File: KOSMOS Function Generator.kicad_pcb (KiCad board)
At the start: 2 copper layers, 96 x 125.6 mm, 96 parts, among them J1 Synth_power_2x5, J2 Conn_01x10_Male, Q1 2N3904, Q2 2N3904, SW1 SW_SPDT, SW2 SW_DPDT_x2, SW3 SW_Push, U1 TL074, U2 TL074, U3 TL074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

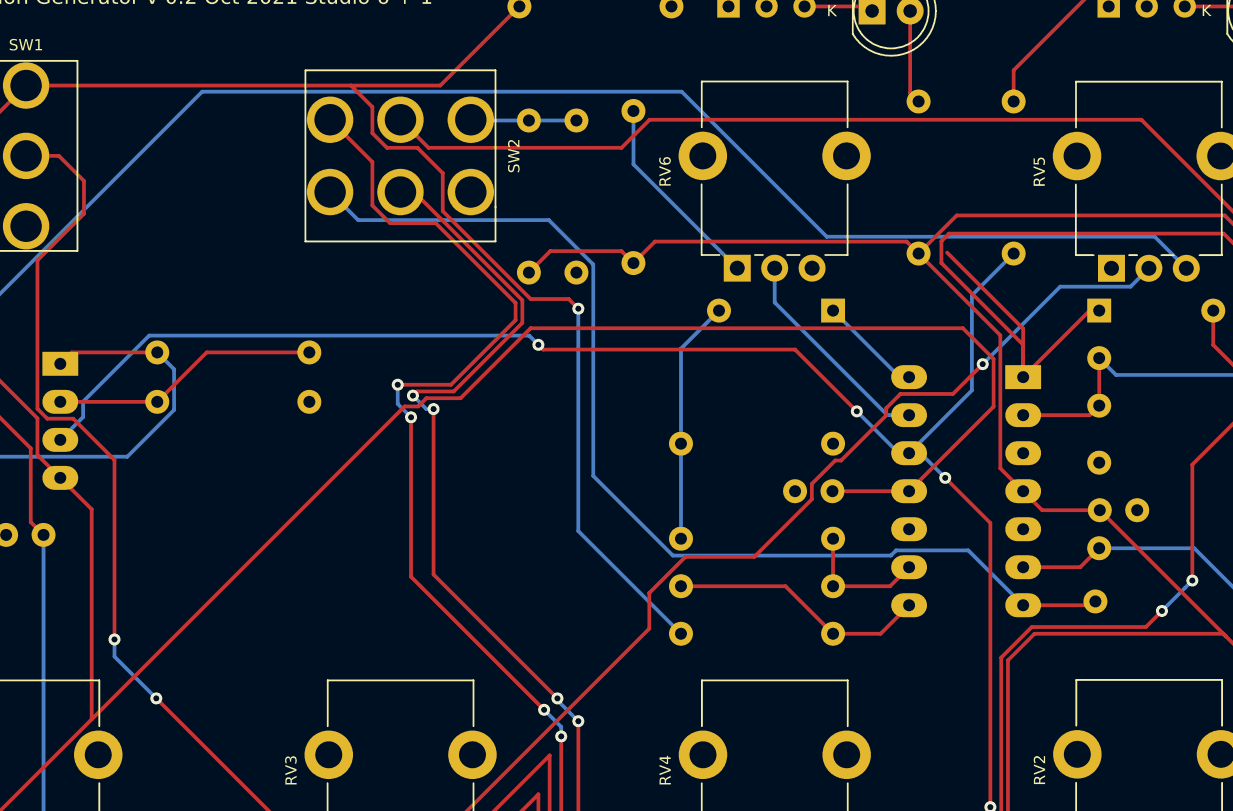
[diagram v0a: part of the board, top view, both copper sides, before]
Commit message: v03 pcb connect ground plane region
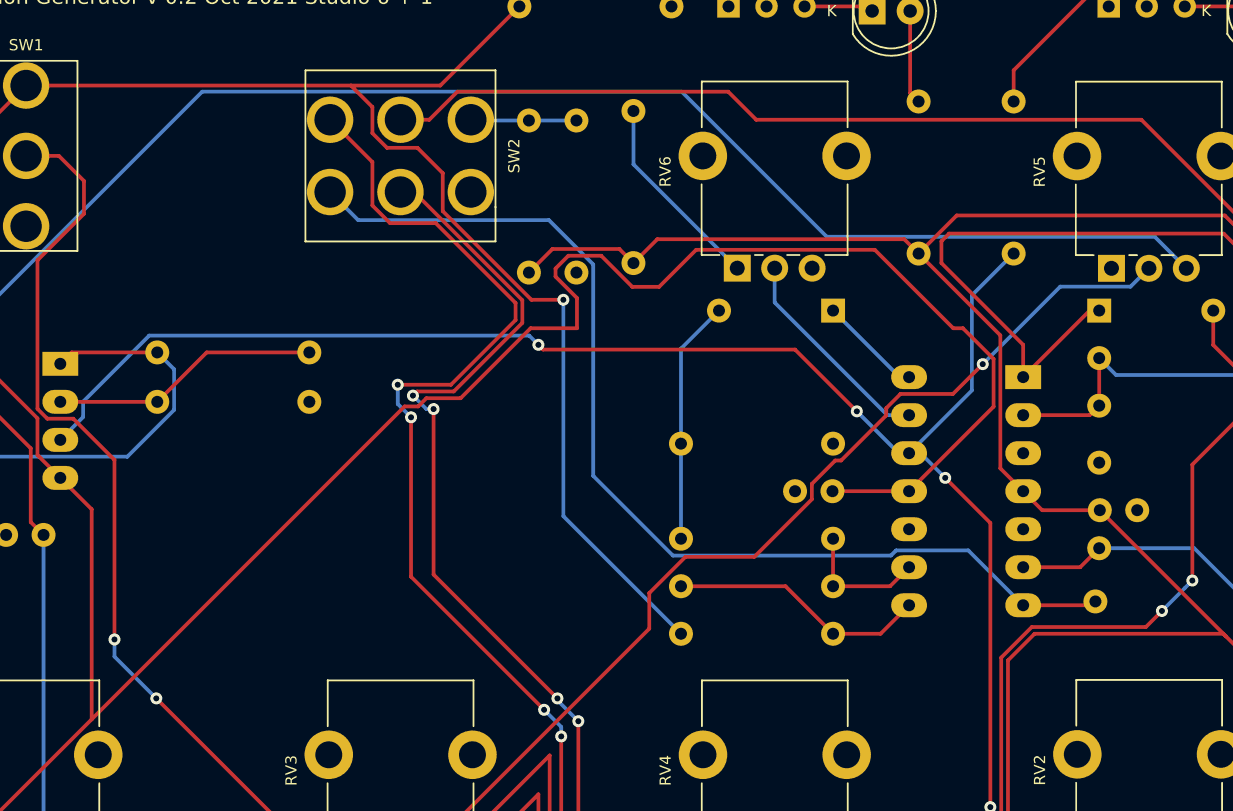
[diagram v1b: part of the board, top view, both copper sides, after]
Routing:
- net -12V: track 360.2 -> 370.6 mm
- net Net-(D6-Pad1): track 61.4 -> 51.0 mm

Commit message: pcb v03
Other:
- board text added: "Function Generator v 0.3 Nov 2021 Studio 6 + 1"
- board text removed: "Function Generator v 0.2 Oct 2021 Studio 6 + 1"
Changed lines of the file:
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@@
     )
   )
-  (gr_text "Function Generator v 0.2 Oct 2021 Studio 6 + 1" (at 40.64 19.05) (layer F.SilkS)
+  (gr_text "Function Generator v 0.3 Nov 2021 Studio 6 + 1" (at 40.64 19.05) (layer F.SilkS)
     (effects (font (size 1 1) (thickness 0.15)))
   )
